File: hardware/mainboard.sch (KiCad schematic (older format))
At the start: 4 parts

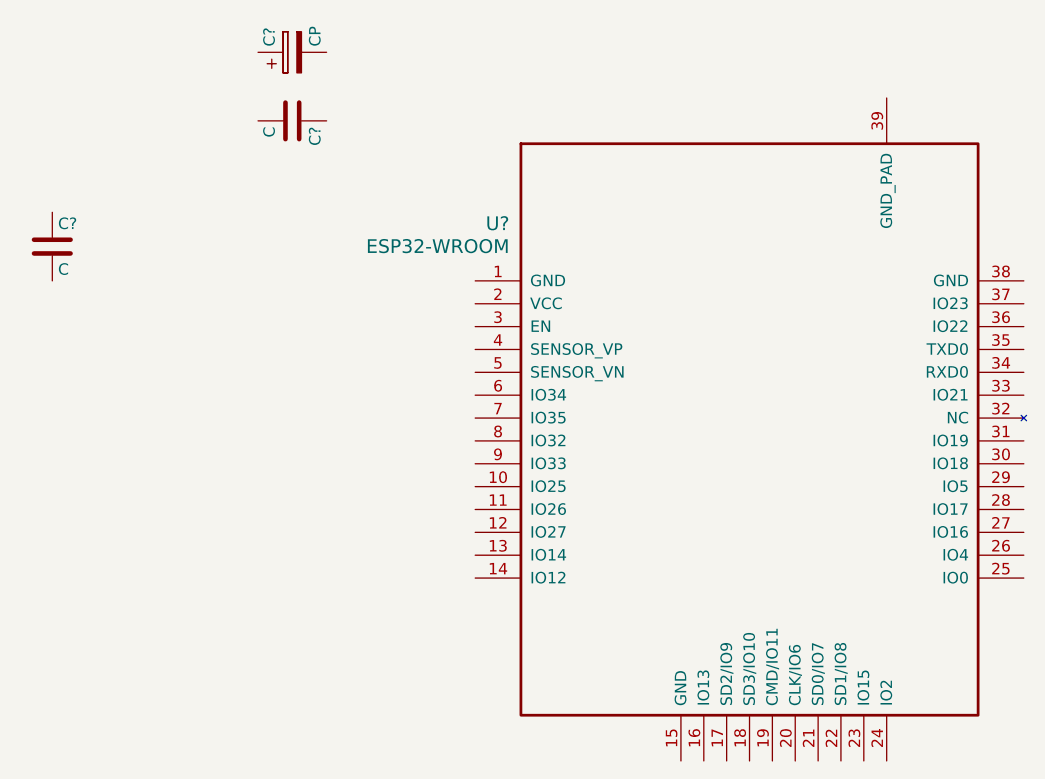
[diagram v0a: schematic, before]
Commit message: Added basic USB and datasheets.
Signed-off-by: Kamil Gardziejczyk <kamil.gardziejczyk@firmwave.com>
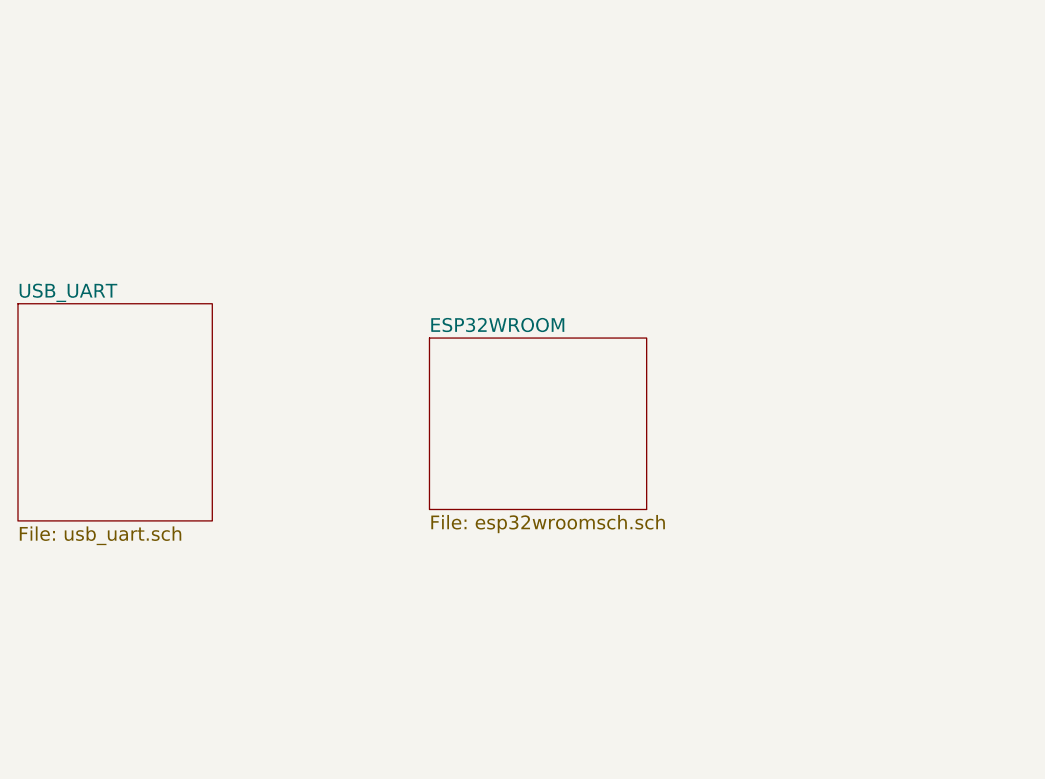
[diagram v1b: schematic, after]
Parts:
- removed C? (x2): C, symbol C
- removed C?: CP, symbol CP
- removed U?: ESP32-WROOM, symbol ESP32-WROOM
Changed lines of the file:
@@
 LIBS:valves
 LIBS:espressif-xess
+LIBS:silabs
+LIBS:mylibrary
+LIBS:ESD_Protection
+LIBS:mainboard-cache
 EELAYER 25 0
 EELAYER END
 $Descr A4 11693 8268
 encoding utf-8
-Sheet 1 1
+Sheet 1 3
 Title ""
 Date ""
@@
 Comment4 ""
 $EndDescr
-$Comp
-L ESP32-WROOM U?
-U 1 1 597777D9
-P 4750 2750
-F 0 "U?" H 4900 3000 60  0000 R CNN
-F 1 "ESP32-WROOM" H 4900 2900 60  0000 R CNN
-F 2 "" H 4750 2750 60  0001 C CNN
-F 3 "" H 4750 2750 60  0001 C CNN
-	1    4750 2750
-	1    0    0    -1
-$EndComp
-$Comp
-L C C?
-U 1 1 5977A5DF
-P 3950 2050
-F 0 "C?" H 3975 2150 50  0000 L CNN
-F 1 "C" H 3975 1950 50  0000 L CNN
-F 2 "" H 3988 1900 50  0001 C CNN
-F 3 "" H 3950 2050 50  0001 C CNN
-	1    3950 2050
-	0    1    1    0
-$EndComp
-$Comp
-L C C?
-U 1 1 5977A6AA
-P 2900 2600
-F 0 "C?" H 2925 2700 50  0000 L CNN
-F 1 "C" H 2925 2500 50  0000 L CNN
-F 2 "" H 2938 2450 50  0001 C CNN
-F 3 "" H 2900 2600 50  0001 C CNN
-	1    2900 2600
-	1    0    0    -1
-$EndComp
-$Comp
-L CP C?
-U 1 1 5977B0F9
-P 3950 1750
-F 0 "C?" H 3975 1850 50  0000 L CNN
-F 1 "CP" H 3975 1650 50  0000 L CNN
-F 2 "" H 3988 1600 50  0001 C CNN
-F 3 "" H 3950 1750 50  0001 C CNN
-	1    3950 1750
-	0    -1   -1   0
-$EndComp
+$Sheet
+S 2750 2850 850  950
+U 597CE1AF
+F0 "USB_UART" 60
+F1 "usb_uart.sch" 60
+$EndSheet
+$Sheet
+S 4550 3000 950  750
+U 597CE33F
+F0 "ESP32WROOM" 60
+F1 "esp32wroomsch.sch" 60
+$EndSheet
 $EndSCHEMATC

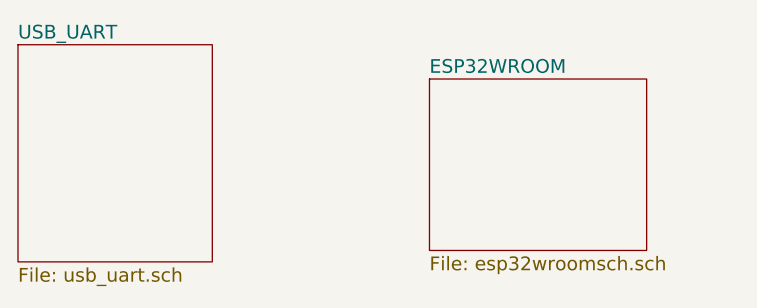
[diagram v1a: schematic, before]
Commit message: Added hierarchical connections and labels clean up.
Signed-off-by: Kamil Gardziejczyk <kamil.gardziejczyk@firmwave.com>
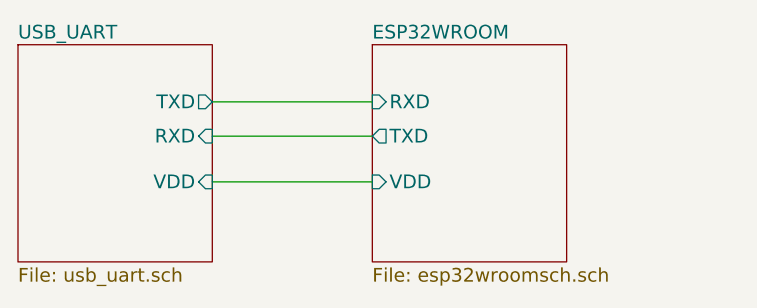
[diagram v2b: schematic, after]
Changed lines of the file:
@@
 F0 "USB_UART" 60
 F1 "usb_uart.sch" 60
+F2 "TXD" O R 3600 3100 60
+F3 "RXD" I R 3600 3250 60
+F4 "VDD" I R 3600 3450 60
 $EndSheet
 $Sheet
-S 4550 3000 950  750
+S 4300 2850 850  950
 U 597CE33F
 F0 "ESP32WROOM" 60
 F1 "esp32wroomsch.sch" 60
+F2 "TXD" O L 4300 3250 60
+F3 "RXD" I L 4300 3100 60
+F4 "VDD" I L 4300 3450 60
 $EndSheet
+Wire Wire Line
+	3600 3100 4300 3100
+Wire Wire Line
+	3600 3250 4300 3250
+Wire Wire Line
+	3600 3450 4300 3450
 $EndSCHEMATC

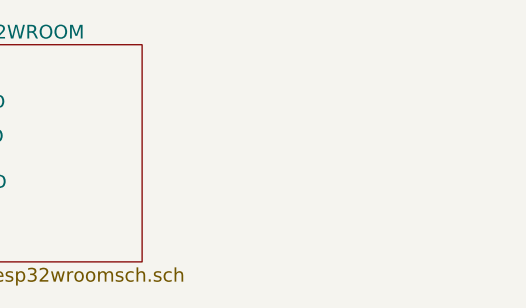
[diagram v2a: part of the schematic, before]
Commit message: Add power sheet and BQ24266 to my library.
Signed-off-by: Kamil Gardziejczyk <kamil.gardziejczyk@firmwave.com>
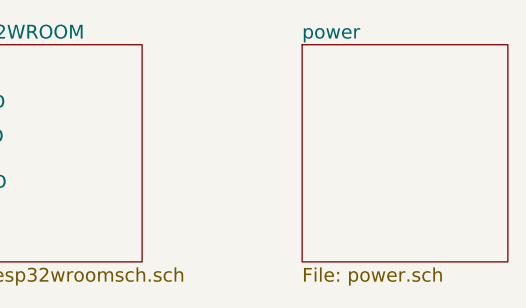
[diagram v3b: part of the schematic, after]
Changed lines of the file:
@@
 $Descr A4 11693 8268
 encoding utf-8
-Sheet 1 3
+Sheet 1 4
 Title ""
 Date ""
@@
 Wire Wire Line
 	3600 3450 4300 3450
+$Sheet
+S 5850 2850 900  950
+U 59862CC8
+F0 "power" 60
+F1 "power.sch" 60
+$EndSheet
 $EndSCHEMATC

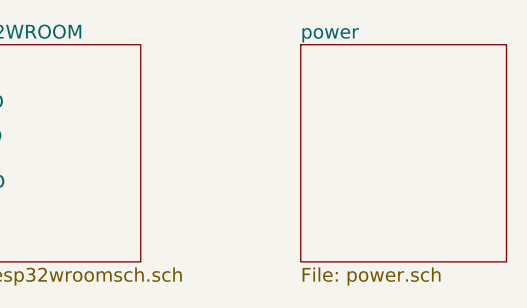
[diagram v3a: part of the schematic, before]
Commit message: Adding TPS63020 to library.
Signed-off-by: Kamil Gardziejczyk <kamil.gardziejczyk@firmwave.com>
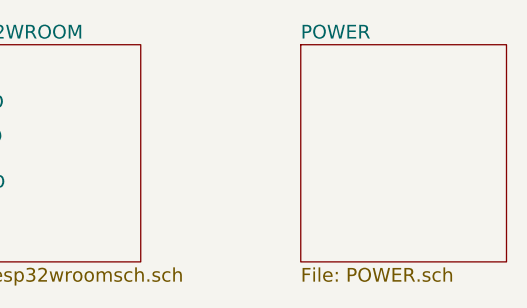
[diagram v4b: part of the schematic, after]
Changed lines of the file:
@@
 S 5850 2850 900  950
 U 59862CC8
-F0 "power" 60
-F1 "power.sch" 60
+F0 "POWER" 60
+F1 "POWER.sch" 60
 $EndSheet
 $EndSCHEMATC
